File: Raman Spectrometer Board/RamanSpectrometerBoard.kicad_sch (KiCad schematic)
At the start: 4 parts

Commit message: Added Anderson Connectors
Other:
- sheet Limi Switches renamed Limit Switches
- added sheet Anderson (anderson.kicad_sch)
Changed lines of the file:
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@@
 	(generator_version "9.0")
 	(paper "A4")
+	(text_box "Im pretty sure the Limit Switches and Motor Encoder are unecessary with the CAN system but im not sure so im leaving it here to be safe. "
+		(exclude_from_sim no)
+		(at 22.86 48.26 0)
+		(size 27.94 15.24)
+		(margins 0.9525 0.9525 0.9525 0.9525)
+		(stroke
+			(width 0)
+			(type solid)
+		)
+		(fill
+			(type none)
+		)
+		(effects
+			(font
+				(size 1.27 1.27)
+			)
+			(justify left top)
+			(href "#1")
+		)
+	)
+	(text_box "I think this just needs a 2 pin molex, but im not sure on specifics, like what voltage the servos need."
+		(exclude_from_sim no)
+		(at 177.8 45.72 0)
+		(size 25.4 15.24)
+		(margins 0.9525 0.9525 0.9525 0.9525)
+		(stroke
+			(width 0)
+			(type solid)
+		)
+		(fill
+			(type none)
+		)
+		(effects
+			(font
+				(size 1.27 1.27)
+			)
+			(justify left top)
+		)
+	)
 	(wire
 		(pts
@@
 	)
 	(sheet
+		(at 257.81 93.98)
+		(size 20.32 20.32)
+		(exclude_from_sim no)
+		(in_bom yes)
+		(on_board yes)
+		(dnp no)
+		(fields_autoplaced yes)
+		(stroke
+			(width 0.1524)
+			(type solid)
+		)
+		(fill
+			(color 0 0 0 0.0000)
+		)
+		(property "Sheetname" "Anderson"
+			(at 257.81 93.2684 0)
+			(effects
+				(font
+					(size 1.27 1.27)
+				)
+				(justify left bottom)
+			)
+		)
+		(property "Sheetfile" "anderson.kicad_sch"
+			(at 257.81 114.8846 0)
+			(effects
+				(font
+					(size 1.27 1.27)
+				)
+				(justify left top)
+			)
+		)
+		(instances
+			(project "RamanSpectrometerBoard"
+				(path "/ab487c59-f066-48f5-a383-99e8eaf806bf"
+					(page "16")
+				)
+			)
+		)
+	)
+	(sheet
 		(at 19.05 45.72)
 		(size 41.91 22.86)
@@
 			(color 0 0 0 0.0000)
 		)
-		(property "Sheetname" "Limi Switches"
+		(property "Sheetname" "Limit Switches"
 			(at 19.05 45.0084 0)
 			(effects

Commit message: Servo Connectors
This definitely, need to be checked.
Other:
- sheet Servo Ports ports: added Servo1, Servo2; removed none
- sheet Teensy ports: added Servo1, Servo2; removed none
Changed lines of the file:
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@@
 		)
 	)
-	(text_box "I think this just needs a 2 pin molex, but im not sure on specifics, like what voltage the servos need."
+	(text_box "Probably need to check this one"
 		(exclude_from_sim no)
 		(at 177.8 45.72 0)
@@
 	(wire
 		(pts
+			(xy 127 57.15) (xy 133.35 57.15)
+		)
+		(stroke
+			(width 0)
+			(type default)
+		)
+	)
+	(wire
+		(pts
 			(xy 60.96 25.4) (xy 68.58 25.4)
+		)
+		(stroke
+			(width 0)
+			(type default)
+		)
+	)
+	(wire
+		(pts
+			(xy 127 53.34) (xy 133.35 53.34)
 		)
 		(stroke
@@
 			)
 		)
+		(pin "Servo1" input
+			(at 133.35 53.34 180)
+			(effects
+				(font
+					(size 1.27 1.27)
+				)
+				(justify left)
+			)
+		)
+		(pin "Servo2" input
+			(at 133.35 57.15 180)
+			(effects
+				(font
+					(size 1.27 1.27)
+				)
+				(justify left)
+			)
+		)
 		(instances
 			(project "RamanSpectrometerBoard"
@@
 			(effects
 				(font
+					(size 1.27 1.27)
+				)
+				(justify right)
+			)
+		)
+		(pin "Servo1" output
+			(at 127 53.34 0)
+			(effects
+				(font
+					(size 1.27 1.27)
+				)
+				(justify right)
+			)
+		)
+		(pin "Servo2" output
+			(at 127 57.15 0)
+			(effects
+				(font

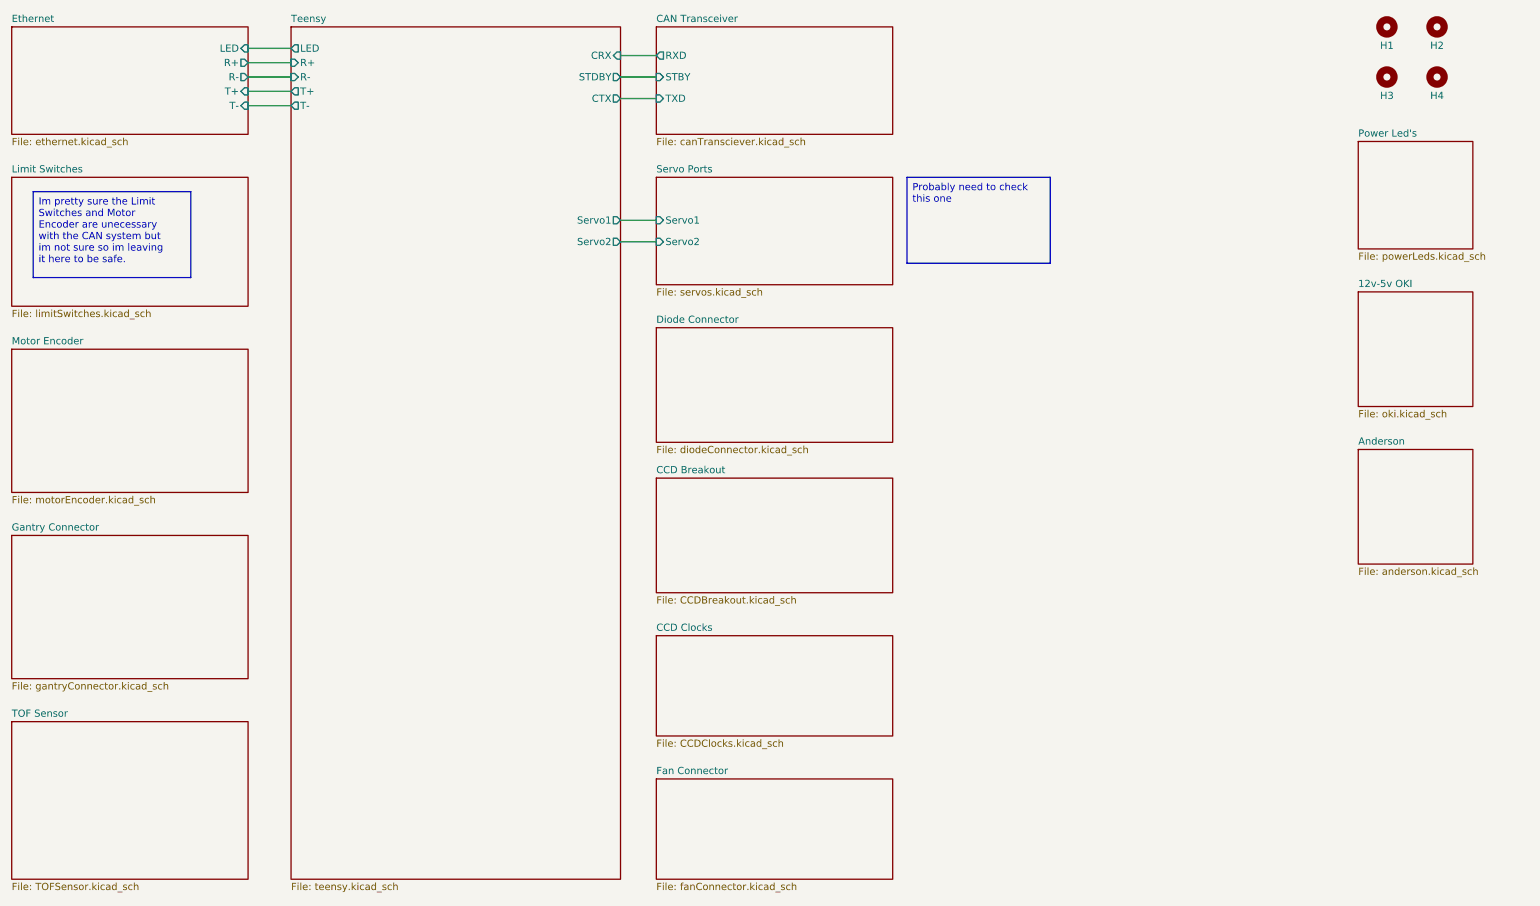
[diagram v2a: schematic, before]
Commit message: Added Diode Connection & Removed Unecessary Pages
Removed, limit switches and motor controller.
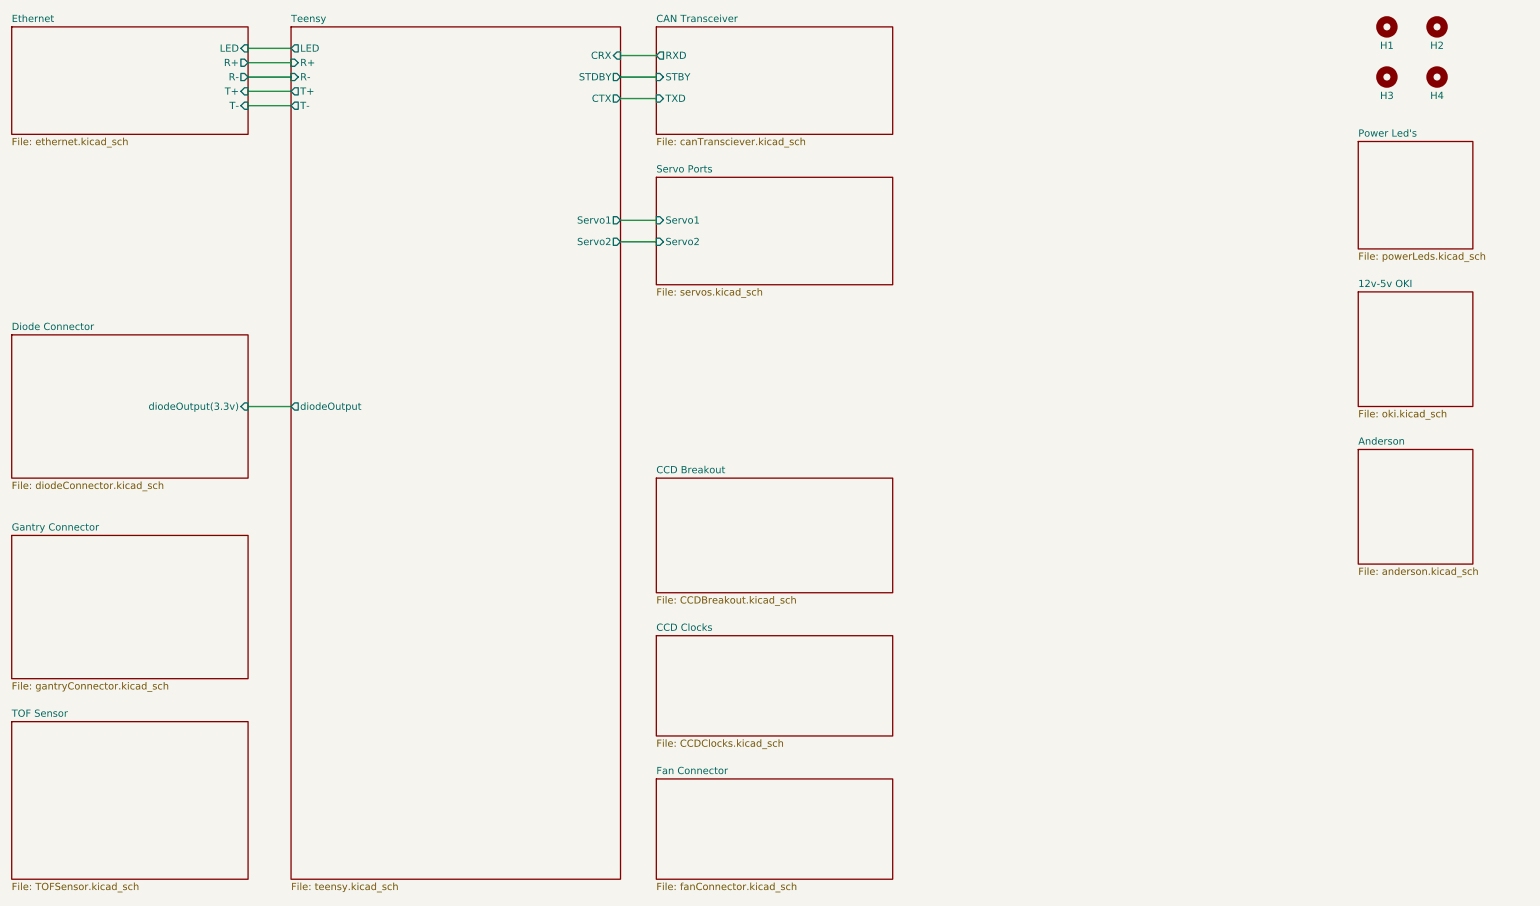
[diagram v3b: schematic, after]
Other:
- removed sheet Limit Switches
- removed sheet Motor Encoder
- sheet Diode Connector ports: added diodeOutput(3.3v); removed none
- sheet Teensy ports: added diodeOutput; removed none
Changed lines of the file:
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@@
 	(generator_version "9.0")
 	(paper "A4")
-	(text_box "Im pretty sure the Limit Switches and Motor Encoder are unecessary with the CAN system but im not sure so im leaving it here to be safe. "
-		(exclude_from_sim no)
-		(at 22.86 48.26 0)
-		(size 27.94 15.24)
-		(margins 0.9525 0.9525 0.9525 0.9525)
-		(stroke
-			(width 0)
-			(type solid)
-		)
-		(fill
-			(type none)
-		)
-		(effects
-			(font
-				(size 1.27 1.27)
-			)
-			(justify left top)
-			(href "#1")
-		)
-	)
-	(text_box "Probably need to check this one"
-		(exclude_from_sim no)
-		(at 177.8 45.72 0)
-		(size 25.4 15.24)
-		(margins 0.9525 0.9525 0.9525 0.9525)
-		(stroke
-			(width 0)
-			(type solid)
-		)
-		(fill
-			(type none)
-		)
-		(effects
-			(font
-				(size 1.27 1.27)
-			)
-			(justify left top)
-		)
-	)
 	(wire
 		(pts
@@
 		(pts
 			(xy 127 53.34) (xy 133.35 53.34)
+		)
+		(stroke
+			(width 0)
+			(type default)
+		)
+	)
+	(wire
+		(pts
+			(xy 60.96 86.36) (xy 68.58 86.36)
 		)
 		(stroke
@@
 	)
 	(sheet
-		(at 19.05 45.72)
-		(size 41.91 22.86)
-		(exclude_from_sim no)
-		(in_bom yes)
-		(on_board yes)
-		(dnp no)
-		(fields_autoplaced yes)
-		(stroke
-			(width 0.1524)
-			(type solid)
-		)
-		(fill
-			(color 0 0 0 0.0000)
-		)
-		(property "Sheetname" "Limit Switches"
-			(at 19.05 45.0084 0)
-			(effects
-				(font
-					(size 1.27 1.27)
-				)
-				(justify left bottom)
-			)
-		)
-		(property "Sheetfile" "limitSwitches.kicad_sch"
-			(at 19.05 69.1646 0)
-			(effects
-				(font
-					(size 1.27 1.27)
-				)
-				(justify left top)
-			)
-		)
-		(instances
-			(project "RamanSpectrometerBoard"
-				(path "/ab487c59-f066-48f5-a383-99e8eaf806bf"
-					(page "9")
-				)
-			)
-		)
-	)
-	(sheet
 		(at 133.35 99.06)
 		(size 41.91 20.32)
@@
 	)
 	(sheet
-		(at 19.05 76.2)
-		(size 41.91 25.4)
-		(exclude_from_sim no)
-		(in_bom yes)
-		(on_board yes)
-		(dnp no)
-		(fields_autoplaced yes)
-		(stroke
-			(width 0.1524)
-			(type solid)
-		)
-		(fill
-			(color 0 0 0 0.0000)
-		)
-		(property "Sheetname" "Motor Encoder"
-			(at 19.05 75.4884 0)
-			(effects
-				(font
-					(size 1.27 1.27)
-				)
-				(justify left bottom)
-			)
-		)
-		(property "Sheetfile" "motorEncoder.kicad_sch"
-			(at 19.05 102.1846 0)
-			(effects
-				(font
-					(size 1.27 1.27)
-				)
-				(justify left top)
-			)
-		)
-		(instances
-			(project "RamanSpectrometerBoard"
-				(path "/ab487c59-f066-48f5-a383-99e8eaf806bf"
-					(page "8")
-				)
-			)
-		)
-	)
-	(sheet
 		(at 19.05 109.22)
 		(size 41.91 25.4)
@@
 	)
 	(sheet
-		(at 133.35 72.39)
-		(size 41.91 20.32)
+		(at 19.05 73.66)
+		(size 41.91 25.4)
 		(exclude_from_sim no)
 		(in_bom yes)
@@
 		)
 		(property "Sheetname" "Diode Connector"
-			(at 133.35 71.6784 0)
+			(at 19.05 72.9484 0)
 			(effects
 				(font
@@
 		)
 		(property "Sheetfile" "diodeConnector.kicad_sch"
-			(at 133.35 93.2946 0)
-			(effects
-				(font
-					(size 1.27 1.27)
-				)
-				(justify left top)
+			(at 19.05 99.6446 0)
+			(effects
+				(font
+					(size 1.27 1.27)
+				)
+				(justify left top)
+			)
+		)
+		(pin "diodeOutput(3.3v)" input
+			(at 60.96 86.36 0)
+			(effects
+				(font
+					(size 1.27 1.27)
+				)
+				(justify right)
 			)
 		)
@@
 			)
 		)
+		(pin "diodeOutput" output
+			(at 68.58 86.36 180)
+			(effects
+				(font
+					(size 1.27 1.27)
+				)
+				(justify left)
+			)
+		)

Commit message: ADC Changes + Delete Fan Connector
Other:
- sheet CCD Breakout ports: added CLK, CLK2, EOS, IN; removed none
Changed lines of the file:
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@@
+			)
+		)
+		(pin "CLK" input
+			(at 133.35 107.95 180)
+			(effects
+				(font
+					(size 1.27 1.27)
+				)
+				(justify left)
+			)
+		)
+		(pin "CLK2" input
+			(at 133.35 113.03 180)
+			(effects
+				(font
+					(size 1.27 1.27)
+				)
+				(justify left)
+			)
+		)
+		(pin "EOS" output
+			(at 133.35 110.49 180)
+			(effects
+				(font
+					(size 1.27 1.27)
+				)
+				(justify left)
+			)
+		)
+		(pin "IN" output
+			(at 133.35 105.41 180)
+			(effects
+				(font
+					(size 1.27 1.27)
+				)
+				(justify left)
 			)
 		)

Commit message: fan connectors
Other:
- sheet Fan Connector ports: added fanOut; removed none
- sheet Teensy ports: added fanOut; removed none
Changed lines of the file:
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@@
+			)
+		)
+		(pin "fanOut" input
+			(at 133.35 161.29 180)
+			(effects
+				(font
+					(size 1.27 1.27)
+				)
+				(justify left)
 			)
 		)
@@
 			)
 		)
+		(pin "fanOut" output
+			(at 127 161.29 0)
+			(effects
+				(font
+					(size 1.27 1.27)
+				)
+				(justify right)
+			)
+		)

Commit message: TOF sensor
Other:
- sheet TOF Sensor ports: added GPID, SCL, SDA; removed none
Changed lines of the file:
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@@
+			)
+		)
+		(pin "GPID" input
+			(at 60.96 154.94 0)
+			(effects
+				(font
+					(size 1.27 1.27)
+				)
+				(justify right)
+			)
+		)
+		(pin "SCL" input
+			(at 60.96 149.86 0)
+			(effects
+				(font
+					(size 1.27 1.27)
+				)
+				(justify right)
+			)
+		)
+		(pin "SDA" input
+			(at 60.96 152.4 0)
+			(effects
+				(font
+					(size 1.27 1.27)
+				)
+				(justify right)
 			)
 		)

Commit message: connect
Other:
- sheet Teensy ports: added GPIP, SCL, SDA; removed none
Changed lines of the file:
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@@
+	(wire
+		(pts
+			(xy 60.96 149.86) (xy 68.58 149.86)
+		)
+		(stroke
+			(width 0)
+			(type default)
+		)
+	)
+	(wire
+		(pts
+			(xy 127 161.29) (xy 133.35 161.29)
+		)
+		(stroke
+			(width 0)
+			(type default)
+		)
+	)
 	(wire
 		(pts
@@
 	(wire
 		(pts
+			(xy 60.96 154.94) (xy 68.58 154.94)
+		)
+		(stroke
+			(width 0)
+			(type default)
+		)
+	)
+	(wire
+		(pts
 			(xy 60.96 27.94) (xy 68.58 27.94)
 		)
@@
 		(pts
 			(xy 127 24.13) (xy 133.35 24.13)
+		)
+		(stroke
+			(width 0)
+			(type default)
+		)
+	)
+	(wire
+		(pts
+			(xy 60.96 152.4) (xy 68.58 152.4)
 		)
 		(stroke
@@
 			)
 		)
+		(pin "GPIP" output
+			(at 68.58 154.94 180)
+			(effects
+				(font
+					(size 1.27 1.27)
+				)
+				(justify left)
+			)
+		)
+		(pin "SCL" output
+			(at 68.58 149.86 180)
+			(effects
+				(font
+					(size 1.27 1.27)
+				)
+				(justify left)
+			)
+		)
+		(pin "SDA" output
+			(at 68.58 152.4 180)
+			(effects
+				(font
+					(size 1.27 1.27)
+				)
+				(justify left)
+			)
+		)

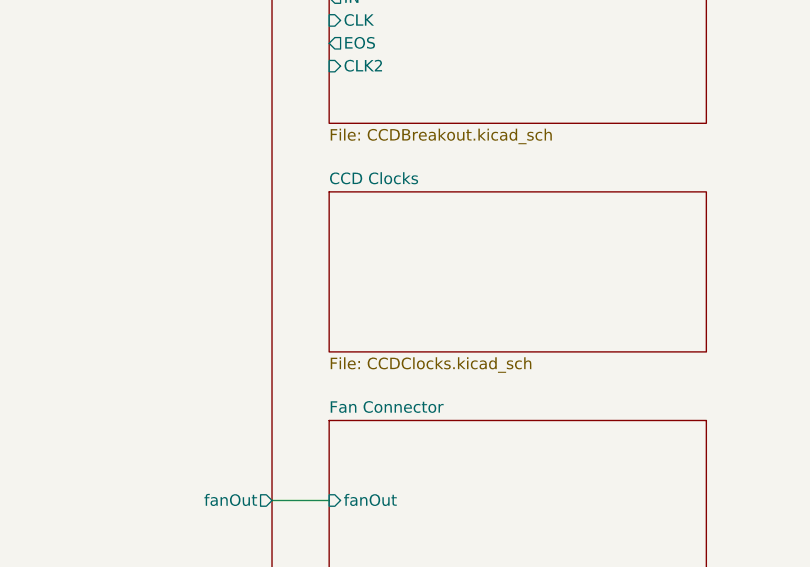
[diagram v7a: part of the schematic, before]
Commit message: CCD clock without teensy connect
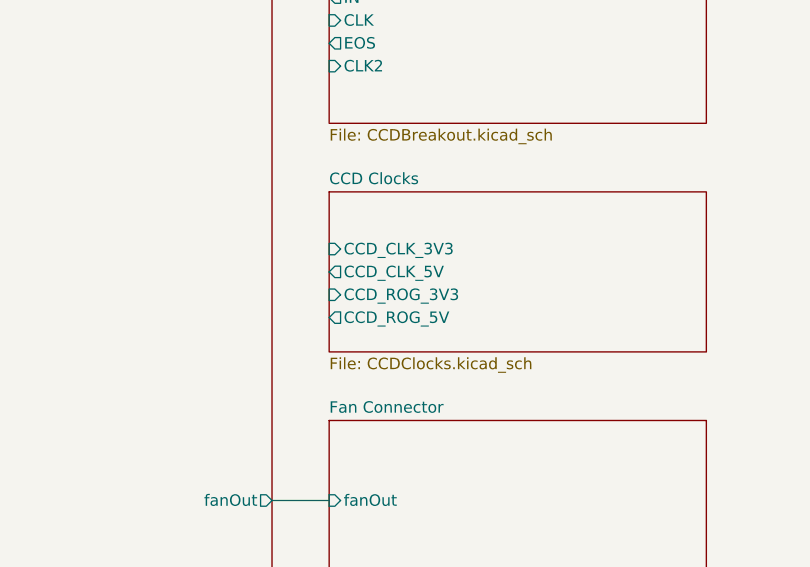
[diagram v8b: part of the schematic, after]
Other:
- sheet CCD Clocks ports: added CCD_CLK_3V3, CCD_CLK_5V, CCD_ROG_3V3, CCD_ROG_5V; removed none
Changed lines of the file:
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@@
+			)
+		)
+		(pin "CCD_CLK_3V3" input
+			(at 133.35 133.35 180)
+			(effects
+				(font
+					(size 1.27 1.27)
+				)
+				(justify left)
+			)
+		)
+		(pin "CCD_CLK_5V" output
+			(at 133.35 135.89 180)
+			(effects
+				(font
+					(size 1.27 1.27)
+				)
+				(justify left)
+			)
+		)
+		(pin "CCD_ROG_3V3" input
+			(at 133.35 138.43 180)
+			(effects
+				(font
+					(size 1.27 1.27)
+				)
+				(justify left)
+			)
+		)
+		(pin "CCD_ROG_5V" output
+			(at 133.35 140.97 180)
+			(effects
+				(font
+					(size 1.27 1.27)
+				)
+				(justify left)
 			)
 		)
